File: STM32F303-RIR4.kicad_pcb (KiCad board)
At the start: 2 copper layers, 114.3 x 106.7 mm, 41 parts, among them J0 CN7, J1 CN10, J101 LCC, J102 LCC, J103 S4 S3 S2 S1 SC, J104 MA MB NA NB, J105 - 12V +, J106 Servo 4, J107 Servo 3, J108 Servo 2, J109 Servo 1, J110 B1 C B2, U101 SN65HVD1050, U102 LM358, U103 TBD62064AFG, U104 TC4428, U105 TC4428, U106 G3VM-61VY4, U107 G3VM-61VY4

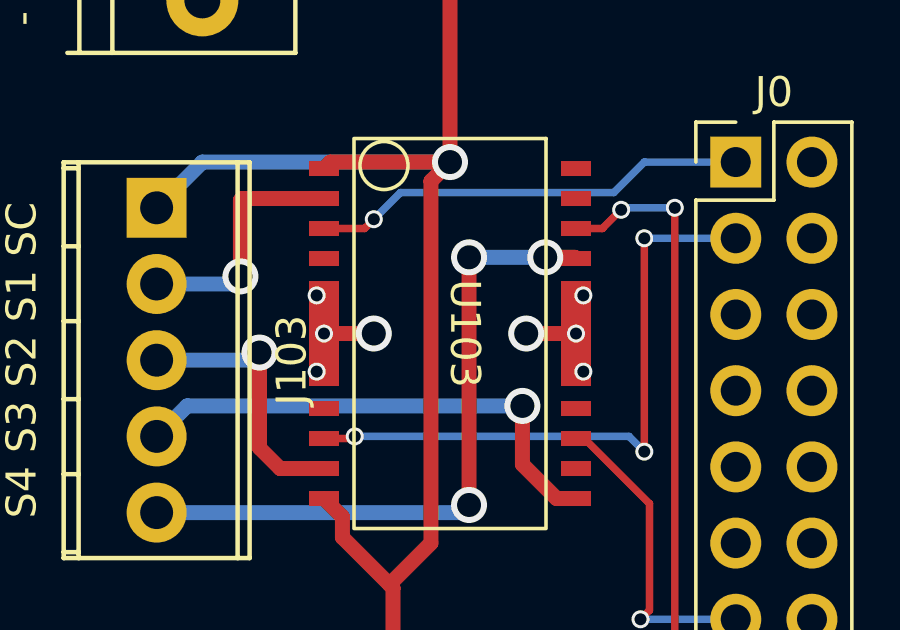
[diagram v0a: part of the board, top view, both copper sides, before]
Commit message: Update board to remove vias in pads.
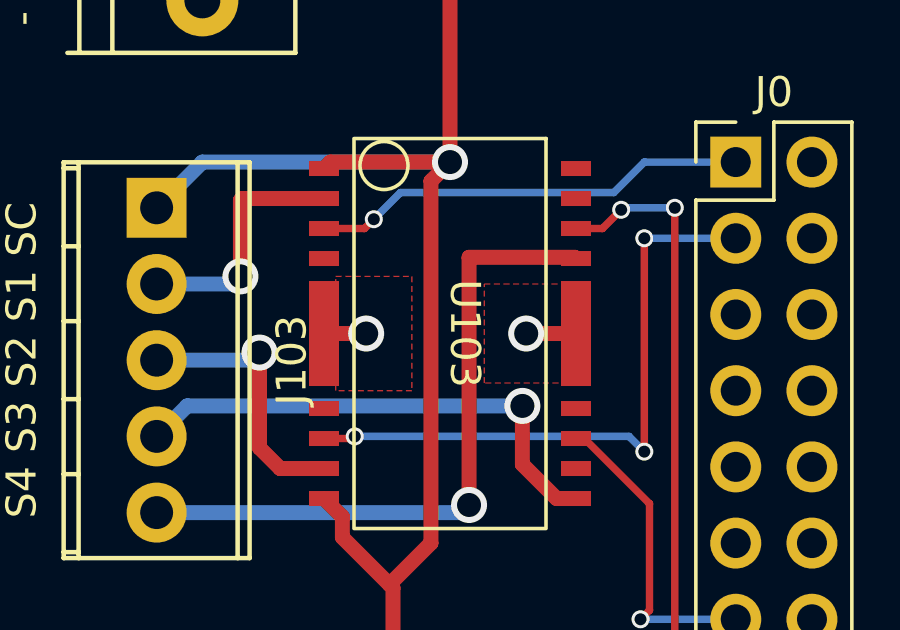
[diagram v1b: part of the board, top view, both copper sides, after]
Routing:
- net GND: track 38.6 -> 31.5 mm, vias 12 -> 6
- net Net-(J103-Pad5): vias 3 -> 1
- added copper zone on F.Cu, net GND
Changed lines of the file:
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@@
   (via (at 62.992 93.98) (size 0.6) (drill 0.4) (layers "F.Cu" "B.Cu") (net 17))
   (segment (start 68.58 93.98) (end 62.992 93.98) (width 0.25) (layer "B.Cu") (net 17))
-  (segment (start 63.255 74.295) (end 63.255 73.27) (width 0.5) (layer "F.Cu") (net 59))
   (segment (start 101.6 112.71) (end 101.6 109.22) (width 0.25) (layer "F.Cu") (net 59))
   (segment (start 139.7 104.76) (end 139.7 105.41) (width 0.25) (layer "F.Cu") (net 59))
   (segment (start 141.224 103.236) (end 139.7 104.76) (width 0.25) (layer "F.Cu") (net 59))
-  (segment (start 63.255 74.295) (end 61.595 74.295) (width 0.5) (layer "F.Cu") (net 59))
   (segment (start 101.6 109.22) (end 101.6 106.68) (width 0.25) (layer "F.Cu") (net 59))
   (segment (start 119.38 123.19) (end 119.38 125.51) (width 0.25) (layer "F.Cu") (net 59))
+  (segment (start 63.255 74.295) (end 61.595 74.295) (width 0.5) (layer "F.Cu") (net 59))
   (segment (start 61.28 91.44) (end 59.69 91.44) (width 0.5) (layer "F.Cu") (net 59))
   (segment (start 101.6 113.735) (end 101.6 112.71) (width 0.25) (layer "F.Cu") (net 59))
   (segment (start 102.87 118.11) (end 102.87 117.085) (width 0.25) (layer "F.Cu") (net 59))
-  (segment (start 54.855 74.295) (end 54.855 73.27) (width 0.5) (layer "F.Cu") (net 59))
   (segment (start 139.7 99.71) (end 141.224 101.234) (width 0.25) (layer "F.Cu") (net 59))
   (segment (start 101.6 115.815) (end 101.6 113.735) (width 0.25) (layer "F.Cu") (net 59))
-  (segment (start 54.855 75.32) (end 54.61 75.565) (width 0.5) (layer "F.Cu") (net 59))
   (segment (start 61.28 99.06) (end 59.69 99.06) (width 0.5) (layer "F.Cu") (net 59))
-  (segment (start 63.255 75.32) (end 63.5 75.565) (width 0.5) (layer "F.Cu") (net 59))
   (segment (start 139.7 99.06) (end 139.7 99.71) (width 0.25) (layer "F.Cu") (net 59))
-  (segment (start 54.855 75.32) (end 54.855 74.295) (width 0.5) (layer "F.Cu") (net 59))
-  (segment (start 63.255 74.295) (end 63.255 75.32) (width 0.5) (layer "F.Cu") (net 59))
+  (segment (start 54.855 74.295) (end 56.261 74.295) (width 0.5) (layer "F.Cu") (net 59))
   (segment (start 102.87 117.085) (end 101.6 115.815) (width 0.25) (layer "F.Cu") (net 59))
   (segment (start 139.7 105.41) (end 138.43 105.41) (width 0.25) (layer "F.Cu") (net 59))
   (segment (start 119.38 125.51) (end 117.89 127) (width 0.25) (layer "F.Cu") (net 59))
-  (segment (start 63.255 73.27) (end 63.5 73.025) (width 0.5) (layer "F.Cu") (net 59))
-  (segment (start 54.855 73.27) (end 54.61 73.025) (width 0.5) (layer "F.Cu") (net 59))
-  (segment (start 54.855 74.295) (end 56.515 74.295) (width 0.5) (layer "F.Cu") (net 59))
   (segment (start 141.224 101.234) (end 141.224 103.236) (width 0.25) (layer "F.Cu") (net 59))
-  (via (at 54.855 74.295) (size 0.6) (drill 0.4) (layers "F.Cu" "B.Cu") (net 59))
   (via (at 59.69 99.06) (size 1.2) (drill 0.8) (layers "F.Cu" "B.Cu") (net 59))
   (via (at 138.43 105.41) (size 0.6) (drill 0.4) (layers "F.Cu" "B.Cu") (net 59))
-  (via (at 54.61 75.565) (size 0.6) (drill 0.4) (layers "F.Cu" "B.Cu") (net 59))
-  (via (at 63.5 75.565) (size 0.6) (drill 0.4) (layers "F.Cu" "B.Cu") (net 59))
   (via (at 101.6 106.68) (size 0.6) (drill 0.4) (layers "F.Cu" "B.Cu") (net 59))
-  (via (at 63.5 73.025) (size 0.6) (drill 0.4) (layers "F.Cu" "B.Cu") (net 59))
-  (via (at 56.515 74.295) (size 1.2) (drill 0.8) (layers "F.Cu" "B.Cu") (net 59))
-  (via (at 63.255 74.295) (size 0.6) (drill 0.4) (layers "F.Cu" "B.Cu") (net 59))
-  (via (at 54.61 73.025) (size 0.6) (drill 0.4) (layers "F.Cu" "B.Cu") (net 59))
+  (via (at 56.261 74.295) (size 1.2) (drill 0.8) (layers "F.Cu" "B.Cu") (net 59))
   (via (at 61.595 74.295) (size 1.2) (drill 0.8) (layers "F.Cu" "B.Cu") (net 59))
   (via (at 59.69 91.44) (size 1.2) (drill 0.8) (layers "F.Cu" "B.Cu") (net 59))
-  (segment (start 63.5 74.05) (end 63.255 74.295) (width 0.5) (layer "B.Cu") (net 59))
-  (segment (start 63.5 73.025) (end 63.5 74.05) (width 0.5) (layer "B.Cu") (net 59))
   (segment (start 92.71 127.22) (end 92.49 127) (width 0.5) (layer "F.Cu") (net 61))
   (segment (start 92.71 131.572) (end 92.71 127.22) (width 0.5) (layer "F.Cu") (net 61))
@@
   (segment (start 52.451 75.184) (end 52.705 74.93) (width 0.5) (layer "B.Cu") (net 76))
   (segment (start 49.276 75.184) (end 52.451 75.184) (width 0.5) (layer "B.Cu") (net 76))
+  (segment (start 62.23 71.755) (end 59.69 71.755) (width 0.5) (layer "F.Cu") (net 77))
   (segment (start 62.23 71.755) (end 63.215 71.755) (width 0.5) (layer "F.Cu") (net 77))
   (segment (start 63.215 71.755) (end 63.255 71.795) (width 0.5) (layer "F.Cu") (net 77))
   (segment (start 59.69 80.01) (end 59.69 71.755) (width 0.5) (layer "F.Cu") (net 77))
-  (via (at 59.69 71.755) (size 1.2) (drill 0.8) (layers "F.Cu" "B.Cu") (net 77))
-  (via (at 62.23 71.755) (size 1.2) (drill 0.8) (layers "F.Cu" "B.Cu") (net 77))
   (via (at 59.69 80.01) (size 1.2) (drill 0.8) (layers "F.Cu" "B.Cu") (net 77))
-  (segment (start 59.69 71.755) (end 62.23 71.755) (width 0.5) (layer "B.Cu") (net 77))
   (segment (start 59.436 80.264) (end 49.276 80.264) (width 0.5) (layer "B.Cu") (net 77))
   (segment (start 59.69 80.01) (end 59.436 80.264) (width 0.5) (layer "B.Cu") (net 77))
@@
   (segment (start 139.7 102.87) (end 137.39 102.87) (width 0.25) (layer "F.Cu") (net 91))
   (segment (start 139.7 96.52) (end 137.39 96.52) (width 0.25) (layer "F.Cu") (net 92))
-  (zone (net 60) (net_name "+5V") (layer "F.Cu") (hatch edge 0.508)
+  (zone (net 59) (net_name "GND") (layer "F.Cu") (hatch edge 0.508)
     (connect_pads yes (clearance 0.508))
     (min_thickness 0.254) (filled_areas_thickness no)
@@
     (polygon
       (pts
+        (xy 62.992 75.946)
+        (xy 60.198 75.946)
+        (xy 60.198 72.644)
+        (xy 62.992 72.644)
+      )
+    )
+  )
+  (zone (net 60) (net_name "+5V") (layer "F.Cu") (hatch edge 0.508)
+    (connect_pads (clearance 0.508))
+    (min_thickness 0.254) (filled_areas_thickness no)
+    (fill yes (thermal_gap 0.508) (thermal_bridge_width 0.508))
+    (polygon
+      (pts
+        (xy 157.48 144.78)
+        (xy 43.18 144.78)
         (xy 43.18 38.1)
         (xy 157.48 38.1)
-        (xy 157.48 144.78)
-        (xy 43.18 144.78)
       )
     )
+  )
+  (zone (net 59) (net_name "GND") (layer "F.Cu") (hatch edge 0.508)
+    (connect_pads yes (clearance 0.508))
+    (min_thickness 0.254) (filled_areas_thickness no)
+    (fill yes (thermal_gap 0.508) (thermal_bridge_width 0.508))
+    (polygon
+      (pts
+        (xy 57.785 76.2)
+        (xy 55.245 76.2)
+        (xy 55.245 72.39)
+        (xy 57.785 72.39)
+      )
+    )

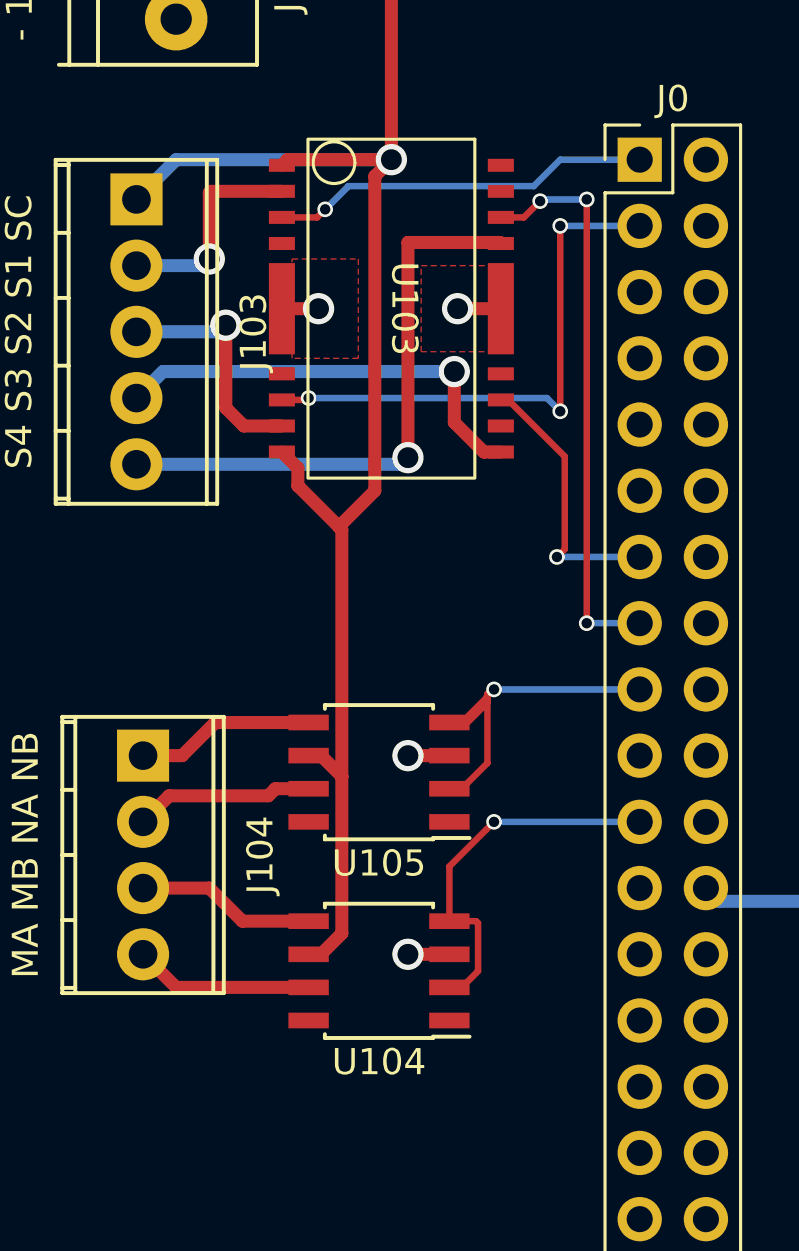
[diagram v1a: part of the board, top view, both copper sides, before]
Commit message: Change Signal I/O pins.
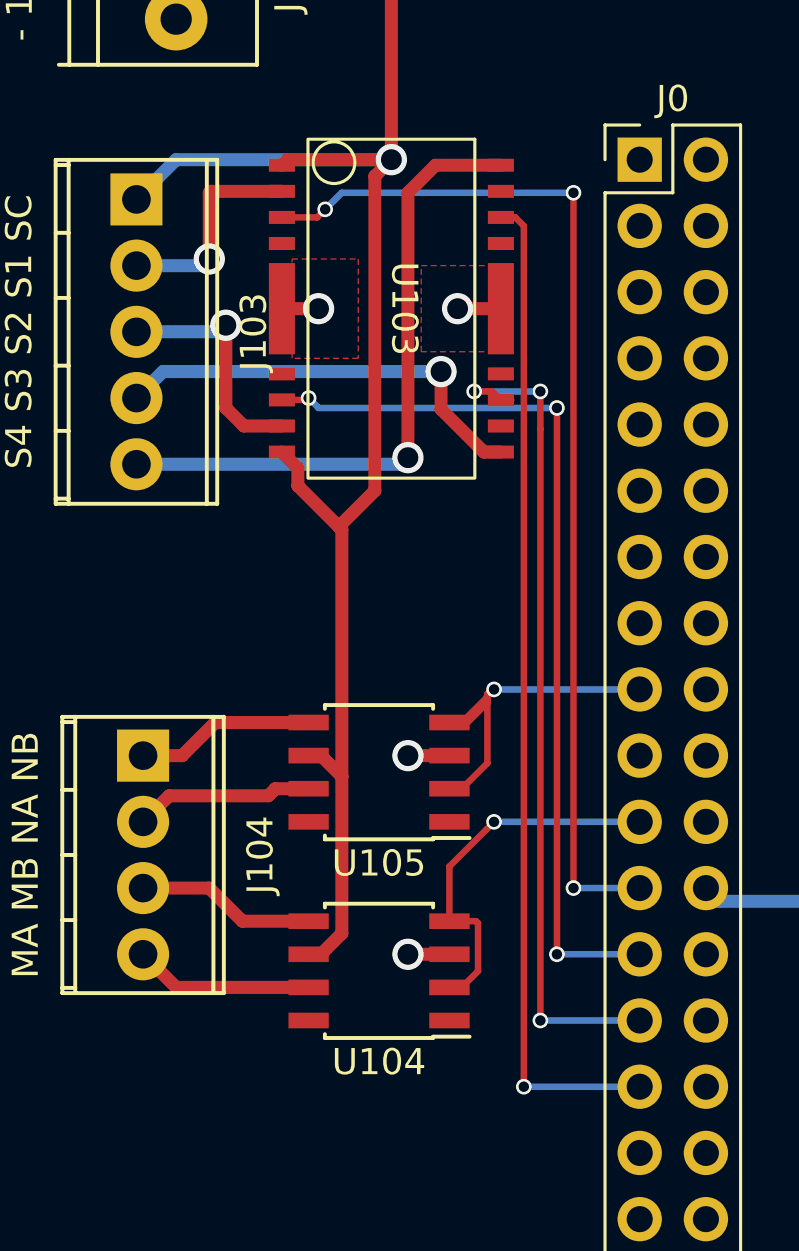
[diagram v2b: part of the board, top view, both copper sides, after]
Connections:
- J0 pad 1: Net-(J0-Pad1) -> unconnected-(J0-Pad1)
- J0 pad 13: Net-(J0-Pad13) -> unconnected-(J0-Pad13)
- J0 pad 15: Net-(J0-Pad15) -> unconnected-(J0-Pad15)
- J0 pad 23: unconnected-(J0-Pad23) -> Net-(U103-Pad3)
- J0 pad 25: unconnected-(J0-Pad25) -> Net-(U103-Pad6)
- J0 pad 27: unconnected-(J0-Pad27) -> Net-(U103-Pad11)
- J0 pad 29: unconnected-(J0-Pad29) -> Net-(U103-Pad14)
- J0 pad 3: Net-(J0-Pad3) -> unconnected-(J0-Pad3)
- U103 pad 11: Net-(J0-Pad13) -> Net-(U103-Pad11)
- U103 pad 13: Net-(J103-Pad5) -> (no net)
- U103 pad 14: Net-(J0-Pad15) -> Net-(U103-Pad14)
- U103 pad 16: (no net) -> Net-(J103-Pad5)
- U103 pad 3: Net-(J0-Pad1) -> Net-(U103-Pad3)
- U103 pad 6: Net-(J0-Pad3) -> Net-(U103-Pad6)
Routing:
- net Net-(U103-Pad3): track 0.00 -> 40.8 mm, vias 0 -> 3
- net Net-(U103-Pad14): track 0.00 -> 38.5 mm, vias 0 -> 1
- net Net-(U103-Pad6): track 0.00 -> 34.9 mm, vias 0 -> 3
- net Net-(U103-Pad11): track 0.00 -> 32.0 mm, vias 0 -> 3
- net Net-(J0-Pad15): track 21.9 -> 0.00 mm, vias 3 -> 0
- net Net-(J0-Pad3): track 21.1 -> 0.00 mm, vias 3 -> 0
- net Net-(J0-Pad1): track 14.6 -> 0.00 mm, vias 1 -> 0
- net Net-(J0-Pad13): track 10.5 -> 0.00 mm, vias 1 -> 0
- net Net-(J103-Pad5): track 22.4 -> 24.7 mm

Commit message: Update board rev.
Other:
- board text added: "(C) Copyright 2023 Robert Heller D/B/A Deepwoods Software STM32F303 CAN BaseBoard Rev B"
- board text removed: "(C) Copyright 2023 Robert Heller D/B/A Deepwoods Software STM32F303 CAN BaseBoard Rev A"
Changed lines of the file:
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@@
   (gr_line (start 43.18 38.1) (end 43.18 144.78) (layer "Edge.Cuts") (width 0.15))
   (gr_line (start 157.48 144.78) (end 157.48 38.1) (layer "Edge.Cuts") (width 0.15))
-  (gr_text "(C) Copyright 2023 Robert Heller\n     D/B/A Deepwoods Software\n     STM32F303 CAN BaseBoard Rev A\n" (at 96.266 52.832) (layer "B.Cu")
+  (gr_text "(C) Copyright 2023 Robert Heller\n     D/B/A Deepwoods Software\n     STM32F303 CAN BaseBoard Rev B\n" (at 96.266 52.832) (layer "B.Cu")
     (effects (font (size 1.5 1.5) (thickness 0.3)) (justify mirror))
   )
@@
   (segment (start 65.405 78.105) (end 56.261 78.105) (width 0.25) (layer "B.Cu") (net 19))
   (segment (start 62.23 77.47) (end 62.93 77.47) (width 0.25) (layer "F.Cu") (net 21))
-  (segment (start 63.655 77.795) (end 63.255 77.795) (width 0.25) (layer "F.Cu") (net 21))
   (segment (start 64.77 101.6) (end 64.77 78.91) (width 0.25) (layer "F.Cu") (net 21))
   (segment (start 64.77 78.91) (end 64.77 77.47) (width 0.25) (layer "F.Cu") (net 21))
@@
         (xy 43.18 144.78)
         (xy 43.18 38.1)
+        (xy 58.42 38.1)
         (xy 157.48 38.1)
       )

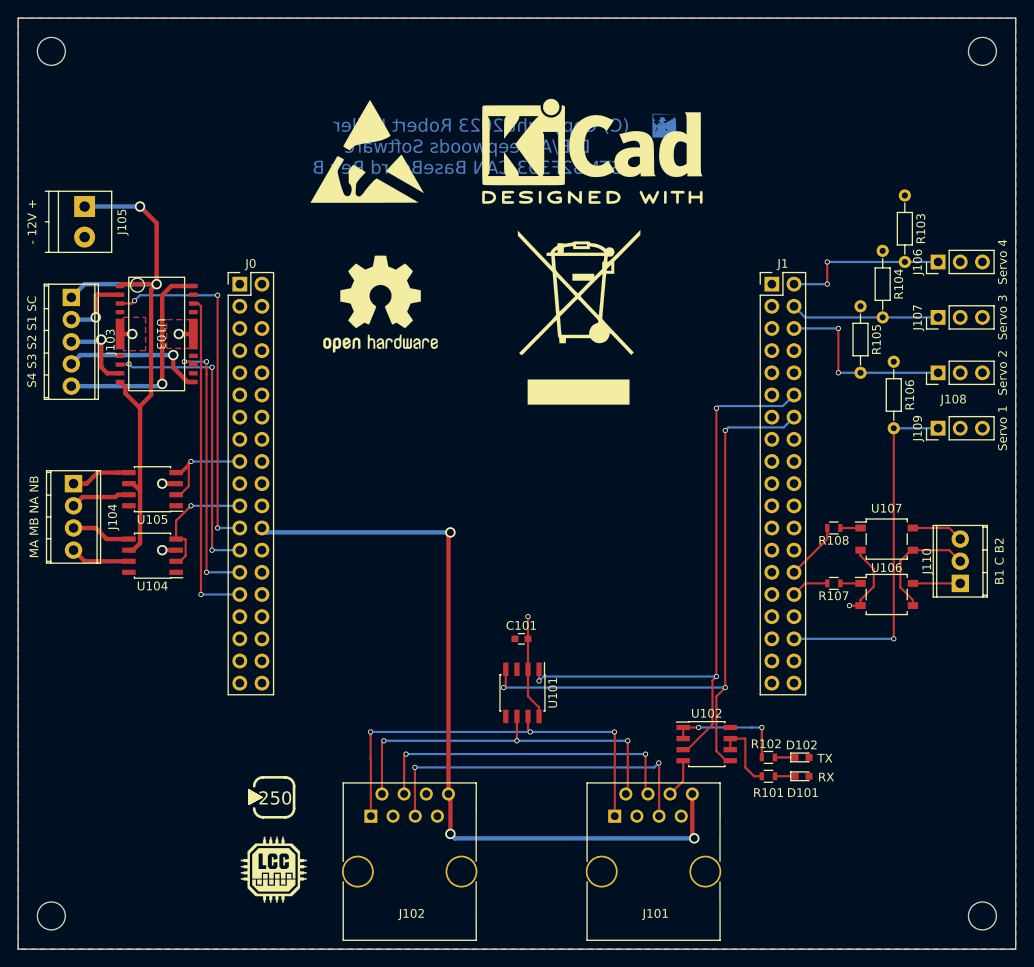
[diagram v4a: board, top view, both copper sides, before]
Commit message: Completed 5V power supply.
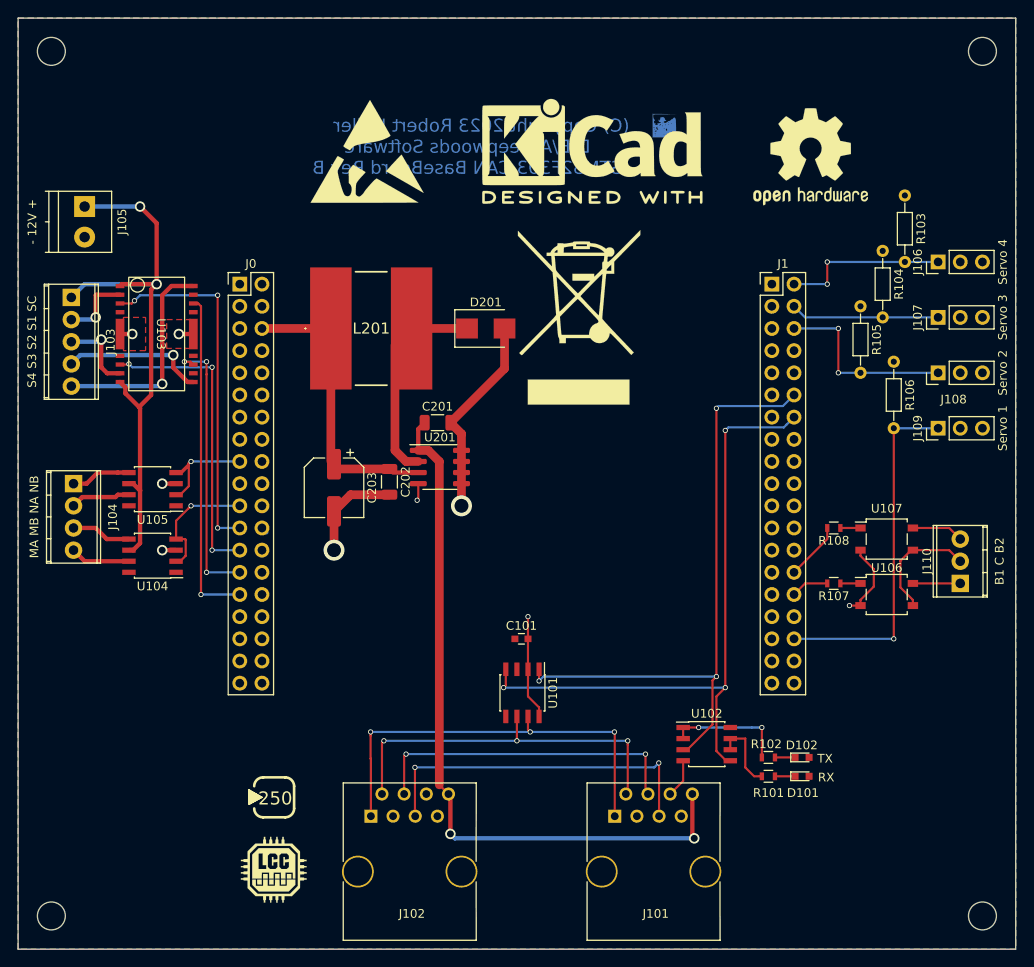
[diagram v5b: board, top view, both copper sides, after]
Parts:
- added C201: 10uf, Capacitor_SMD:C_1206_3216Metric, F.Cu at (91.2, 84.5)
- added C202: 22uf 6.3V, Capacitor_SMD:C_1206_3216Metric, F.Cu at (85.7, 91.2)
- added C203: 220uf 20% 10V, Capacitor_SMD:CP_Elec_6.3x7.7, F.Cu at (79.4, 91.9)
- added D201: SK23TR, Diode_SMD:D_SMB, F.Cu at (96.8, 73.7)
- added L201: 47uh, inductors:SDR1307A470K, F.Cu at (83.6, 73.7)
- added U201: AP1509-50, Package_SO:SOIC-8_3.9x4.9mm_P1.27mm, F.Cu at (91.5, 89.5)
- moved REF*** 52.1 mm to (134.0, 54.0)
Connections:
- J0 pad 24: /LCC_CAN_12V -> unconnected-(J0-Pad24)
- J0 pad 6: unconnected-(J0-Pad6) -> E5V
- J101 pad 8: /LCC_CAN_12V -> LCC_CAN_12V
- J102 pad 8: /LCC_CAN_12V -> LCC_CAN_12V
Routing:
- net /LCC_CAN_12V: track 89.8 -> 0.00 mm, vias 3 -> 0
- net LCC_CAN_12V: track 0.00 -> 82.9 mm, vias 0 -> 2
- net GND: track 31.5 -> 68.5 mm, vias 6 -> 9
- net E5V: track 0.00 -> 33.6 mm
- net Net-(D201-Pad1): track 0.00 -> 24.3 mm
- net unconnected-(J0-Pad24): track 0.00 -> 0.72 mm
